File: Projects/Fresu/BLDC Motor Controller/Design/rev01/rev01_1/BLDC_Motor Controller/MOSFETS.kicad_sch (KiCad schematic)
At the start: 32 parts, among them J4 7461084, J5 7461084, J6 7461084, Q1 HSBA15810C, Q2 HSBA15810C, Q3 HSBA15810C, Q4 HSBA15810C, Q5 HSBA15810C, Q6 HSBA15810C

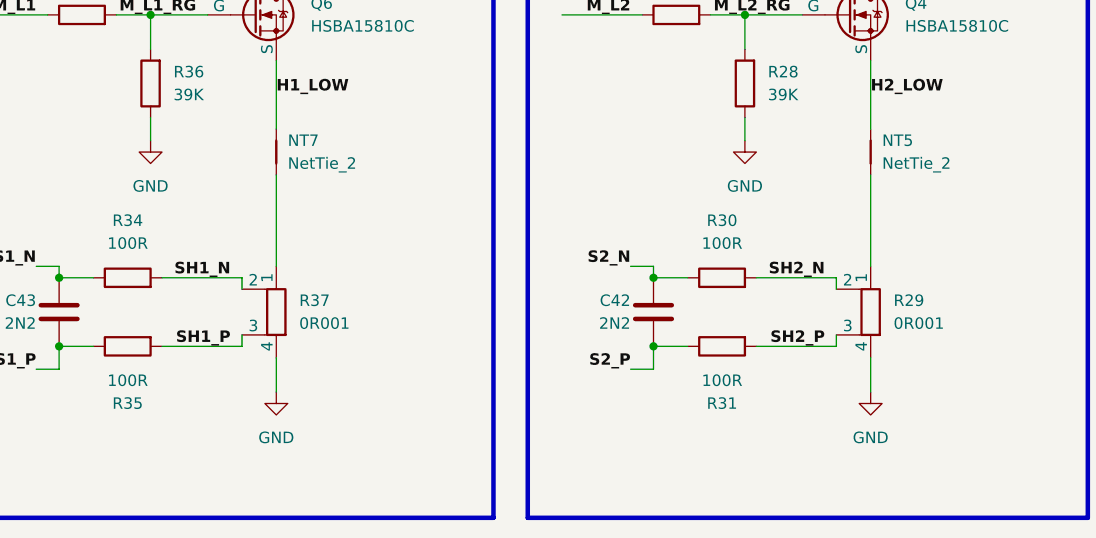
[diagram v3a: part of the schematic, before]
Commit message: Update 14
Added 4 mounting holes, imported all components into PCB project, created board outline
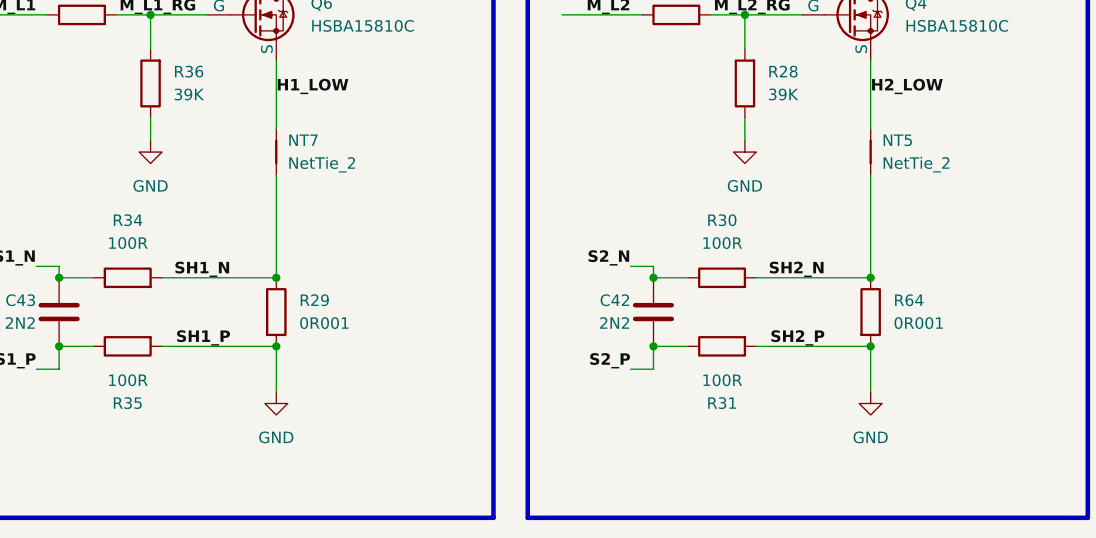
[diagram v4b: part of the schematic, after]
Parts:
- removed R29, R37: 0R001, DF_ESC_Footprint_Library:RES-SMD_L7.0-W6.7, symbol Device:R_Shunt
- added R29, R64: 0R001, DF_ESC_Footprint_Library:RES-SMD_L7.0-W6.7, symbol Device:R
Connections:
- net SH1_P is gone; now on net GND: R35.2
- net SH2_P is gone; now on net GND: R31.2
- net GND: now also R29.2, R64.2
- net SH1_N: now also NT7.1, R29.1
- net SH2_N: now also NT5.1, R64.1
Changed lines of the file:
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@@
   (junction (at 124.46 116.84) (diameter 0) (color 0 0 0 0)
   )
+  (junction (at 148.59 116.84) (diameter 0) (color 0 0 0 0)
+  )
   (junction (at 199.39 99.06) (diameter 0) (color 0 0 0 0)
   )
+  (junction (at 148.59 124.46) (diameter 0) (color 0 0 0 0)
+  )
   (junction (at 124.46 124.46) (diameter 0) (color 0 0 0 0)
   )
   (junction (at 148.59 74.93) (diameter 0) (color 0 0 0 0)
   )
+  (junction (at 82.55 124.46) (diameter 0) (color 0 0 0 0)
+  )
   (junction (at 58.42 116.84) (diameter 0) (color 0 0 0 0)
   )
@@
   (junction (at 82.55 74.93) (diameter 0) (color 0 0 0 0)
   )
+  (junction (at 82.55 116.84) (diameter 0) (color 0 0 0 0)
+  )
   (wire (pts (xy 58.42 116.84) (xy 62.23 116.84))
     (stroke (width 0) (type default))
@@
     (stroke (width 0) (type default))
   )
-  (wire (pts (xy 148.59 105.41) (xy 148.59 115.57))
+  (wire (pts (xy 148.59 105.41) (xy 148.59 116.84))
     (stroke (width 0) (type default))
   )
@@
     (stroke (width 0) (type default))
   )
-  (wire (pts (xy 78.74 116.84) (xy 78.74 118.11))
-    (stroke (width 0) (type default))
-  )
-  (wire (pts (xy 69.85 116.84) (xy 78.74 116.84))
+  (wire (pts (xy 69.85 116.84) (xy 82.55 116.84))
     (stroke (width 0) (type default))
   )
@@
     (stroke (width 0.5) (type default))
   )
-  (wire (pts (xy 69.85 124.46) (xy 78.74 124.46))
-    (stroke (width 0) (type default))
-  )
-  (wire (pts (xy 144.78 124.46) (xy 144.78 123.19))
+  (wire (pts (xy 69.85 124.46) (xy 82.55 124.46))
     (stroke (width 0) (type default))
   )
@@
     (stroke (width 0.5) (type default))
   )
-  (wire (pts (xy 135.89 116.84) (xy 144.78 116.84))
-    (stroke (width 0) (type default))
-  )
   (wire (pts (xy 148.59 74.93) (xy 148.59 82.55))
     (stroke (width 0) (type default))
@@
     (stroke (width 0.5) (type default))
   )
+  (wire (pts (xy 135.89 116.84) (xy 148.59 116.84))
+    (stroke (width 0) (type default))
+  )
   (polyline (pts (xy 41.91 19.05) (xy 41.91 55.88))
     (stroke (width 0.5) (type default))
@@
     (stroke (width 0) (type default))
   )
-  (wire (pts (xy 144.78 116.84) (xy 144.78 118.11))
-    (stroke (width 0) (type default))
-  )
   (polyline (pts (xy 243.84 58.42) (xy 243.84 44.45))
     (stroke (width 0.5) (type default))
@@
     (stroke (width 0.5) (type default))
   )
-  (wire (pts (xy 82.55 105.41) (xy 82.55 115.57))
+  (wire (pts (xy 82.55 105.41) (xy 82.55 116.84))
     (stroke (width 0) (type default))
   )
@@
     (stroke (width 0) (type default))
   )
-  (wire (pts (xy 78.74 124.46) (xy 78.74 123.19))
-    (stroke (width 0) (type default))
-  )
   (wire (pts (xy 199.39 99.06) (xy 199.39 102.87))
     (stroke (width 0) (type default))
@@
     (stroke (width 0) (type default))
   )
-  (wire (pts (xy 135.89 124.46) (xy 144.78 124.46))
+  (wire (pts (xy 135.89 124.46) (xy 148.59 124.46))
     (stroke (width 0) (type default))
   )
@@
     (stroke (width 0) (type default))
   )
-  (wire (pts (xy 82.55 125.73) (xy 82.55 129.54))
+  (wire (pts (xy 82.55 124.46) (xy 82.55 129.54))
     (stroke (width 0) (type default))
   )
@@
     (stroke (width 0.5) (type default))
   )
-  (wire (pts (xy 148.59 125.73) (xy 148.59 129.54))
+  (wire (pts (xy 148.59 124.46) (xy 148.59 129.54))
     (stroke (width 0) (type default))
   )
@@
     )
   )
+  (symbol (lib_id "Device:R") (at 82.55 120.65 0) (unit 1)
+    (in_bom yes) (on_board yes) (dnp no) (fields_autoplaced)
+    (property "Reference" "R29" (at 85.09 119.38 0)
+      (effects (font (size 1.27 1.27)) (justify left))
+    )
+    (property "Value" "0R001" (at 85.09 121.92 0)
+      (effects (font (size 1.27 1.27)) (justify left))
+    )
+    (property "Footprint" "DF_ESC_Footprint_Library:RES-SMD_L7.0-W6.7" (at 80.772 120.65 90)
+      (effects (font (size 1.27 1.27)) hide)
+    )
+    (property "Datasheet" "~" (at 82.55 120.65 0)
+      (effects (font (size 1.27 1.27)) hide)
+    )
+    (pin "1")
+    (pin "2")
+    (instances
+      (project "BLDC_Motor Controller"
+        (path "/e63e39d7-6ac0-4ffd-8aa3-1841a4541b55/6ff318f8-ab62-4d6d-8e81-6536cd3472e5"
+          (reference "R29") (unit 1)
+        )
+      )
+    )
+  )
   (symbol (lib_id "Device:NetTie_2") (at 213.36 114.3 90) (unit 1)
     (in_bom no) (on_board yes) (dnp no) (fields_autoplaced)
@@
     )
   )
+  (symbol (lib_id "Device:R") (at 148.59 120.65 0) (unit 1)
+    (in_bom yes) (on_board yes) (dnp no) (fields_autoplaced)
+    (property "Reference" "R64" (at 151.13 119.38 0)
+      (effects (font (size 1.27 1.27)) (justify left))
+    )
+    (property "Value" "0R001" (at 151.13 121.92 0)
+      (effects (font (size 1.27 1.27)) (justify left))
+    )
+    (property "Footprint" "DF_ESC_Footprint_Library:RES-SMD_L7.0-W6.7" (at 146.812 120.65 90)
+      (effects (font (size 1.27 1.27)) hide)
+    )
+    (property "Datasheet" "~" (at 148.59 120.65 0)
+      (effects (font (size 1.27 1.27)) hide)
+    )
+    (pin "1")
+    (pin "2")
+    (instances
+      (project "BLDC_Motor Controller"
+        (path "/e63e39d7-6ac0-4ffd-8aa3-1841a4541b55/6ff318f8-ab62-4d6d-8e81-6536cd3472e5"
+          (reference "R64") (unit 1)
+        )
+      )
+    )
+  )
   (symbol (lib_id "Device:R") (at 132.08 116.84 90) (unit 1)
     (in_bom yes) (on_board yes) (dnp no) (fields_autoplaced)
@@
     )
   )
-  (symbol (lib_id "Device:R_Shunt") (at 148.59 120.65 0) (mirror y) (unit 1)
-    (in_bom yes) (on_board yes) (dnp no) (fields_autoplaced)
-    (property "Reference" "R29" (at 151.13 119.38 0)
-      (effects (font (size 1.27 1.27)) (justify right))
-    )
-    (property "Value" "0R001" (at 151.13 121.92 0)
-      (effects (font (size 1.27 1.27)) (justify right))
-    )
-    (property "Footprint" "DF_ESC_Footprint_Library:RES-SMD_L7.0-W6.7" (at 150.368 120.65 90)
-      (effects (font (size 1.27 1.27)) hide)
-    )
-    (property "Datasheet" "~" (at 148.59 120.65 0)
-      (effects (font (size 1.27 1.27)) hide)
-    )
-    (pin "4")
-    (pin "1")
-    (pin "2")
-    (pin "3")
-    (instances
-      (project "BLDC_Motor Controller"
-        (path "/e63e39d7-6ac0-4ffd-8aa3-1841a4541b55/6ff318f8-ab62-4d6d-8e81-6536cd3472e5"
-          (reference "R29") (unit 1)
-        )
-      )
-    )
-  )
   (symbol (lib_id "Device:R") (at 191.77 73.66 90) (unit 1)
     (in_bom yes) (on_board yes) (dnp no) (fields_autoplaced)
@@
         )
       )
-    )
-  )
-  (symbol (lib_id "Device:R_Shunt") (at 82.55 120.65 0) (mirror y) (unit 1)
-    (in_bom yes) (on_board yes) (dnp no) (fields_autoplaced)
-    (property "Reference" "R37" (at 85.09 119.38 0)
-      (effects (font (size 1.27 1.27)) (justify right))
-    )
-    (property "Value" "0R001" (at 85.09 121.92 0)
-      (effects (font (size 1.27 1.27)) (justify right))
-    )
-    (property "Footprint" "DF_ESC_Footprint_Library:RES-SMD_L7.0-W6.7" (at 84.328 120.65 90)
-      (effects (font (size 1.27 1.27)) hide)
-    )
-    (property "Datasheet" "~" (at 82.55 120.65 0)
-      (effects (font (size 1.27 1.27)) hide)
-    )
-    (pin "4")
-    (pin "1")
-    (pin "2")
-    (pin "3")
-    (instances
-      (project "BLDC_Motor Controller"
-        (path "/e63e39d7-6ac0-4ffd-8aa3-1841a4541b55/6ff318f8-ab62-4d6d-8e81-6536cd3472e5"
-          (reference "R37") (unit 1)
-        )
-      )

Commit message: Update 15
Fixing some schematic errors

initial layout of larger component complete
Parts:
- C42: renamed from C43; value 2N2 -> 2n2
- C43: renamed from C42; value 2N2 -> 2n2
- renumbered NT6 to NT2, NT7 to NT3, NT2 to NT6, NT3 to NT7, Q5 to Q1, Q6 to Q2, Q1 to Q5, Q2 to Q6, R32 to R24, R33 to R25, R34 to R26, R35 to R27, R36 to R28, R26 to R30, R27 to R31, R30 to R32, R31 to R33, R28 to R34, R64 to R35, R23 to R36, R24 to R37, R25 to R38

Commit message: Update 16
Almost finished placing all the components on the board as rough placement
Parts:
- removed NT7: NetTie_2, DF_ESC_Footprint_Library:NetTie_SMD_Pad_3.00mm, symbol Device:NetTie_2
- removed Q1, Q2, Q3, Q4, Q5, Q6: HSBA15810C, Package_DFN_QFN:PQFN-8-EP_6x5mm_P1.27mm_Generic, symbol Simulation_SPICE:NMOS
- added NT7, NT8, NT9: Net_Tie_PWR, DF_ESC_Footprint_Library:NetTie_SMD_Pad_6.00mm, symbol DF_ESC_Symbol_Library:Net_Tie_PWR
- added Q1, Q2, Q3, Q4, Q5, Q6: HSBA15810C, DF_ESC_Footprint_Library:PQFN-8_L6.0-W5.0-P1.27-LS6.0-BL, symbol DF_ESC_Symbol_Library:HSBA15810C
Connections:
- net +VDC: now also Q1.5 (D), Q1.6 (D), Q1.7 (D), Q1.8 (D), Q1.9 (D), Q3.5 (D), Q3.6 (D), Q3.7 (D), Q3.8 (D), Q3.9 (D), Q5.5 (D), Q5.6 (D), Q5.7 (D), Q5.8 (D), Q5.9 (D)
- net GND: now also NT7.1, NT8.1, NT9.1; no longer R27.2, R29.2, R33.2, R35.2
- net H1_LOW: now also Q2.1 (S), Q2.2 (S), Q2.3 (S)
- net H2_LOW: now also Q4.1 (S), Q4.2 (S), Q4.3 (S)
- net H3_LOW: now also NT7.2, Q6.1 (S), Q6.2 (S), Q6.3 (S)
- net M_H1_RG: now also Q1.4 (G)
- net M_H2_RG: now also Q3.4 (G)
- net M_H3_RG: now also Q5.4 (G)
- net M_L1_RG: now also Q2.4 (G)
- net M_L2_RG: now also Q4.4 (G)
- net M_L3_RG: now also Q6.4 (G)
- net PHASE_1: now also Q1.1 (S), Q1.2 (S), Q1.3 (S), Q2.5 (D), Q2.6 (D), Q2.7 (D), Q2.8 (D), Q2.9 (D)
- net PHASE_2: now also Q3.1 (S), Q3.2 (S), Q3.3 (S), Q4.5 (D), Q4.6 (D), Q4.7 (D), Q4.8 (D), Q4.9 (D)
- net PHASE_3: now also Q5.1 (S), Q5.2 (S), Q5.3 (S), Q6.5 (D), Q6.6 (D), Q6.7 (D), Q6.8 (D), Q6.9 (D)
- net SH1_N: now also R29.2; no longer R29.1
- net SH2_N: now also R35.2; no longer R35.1
- new net SH1_P: NT8.2, R27.2, R29.1
- new net SH2_P: NT9.2, R33.2, R35.1
